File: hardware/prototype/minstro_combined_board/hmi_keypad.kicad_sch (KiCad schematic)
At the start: 34 parts, among them SW401 POWER, SW402 SW_A1, SW403 SW_A2, SW404 SW_A3, SW405 SW_A4, SW406 SW_B1, SW407 SW_B2, SW408 SW_B3, SW409 SW_B4, SW410 SW_C1, SW411 SW_C2, SW412 SW_C3, SW413 SW_C4, SW414 SW_D1, SW415 SW_D2, SW416 SW_D3, SW417 SW_D4

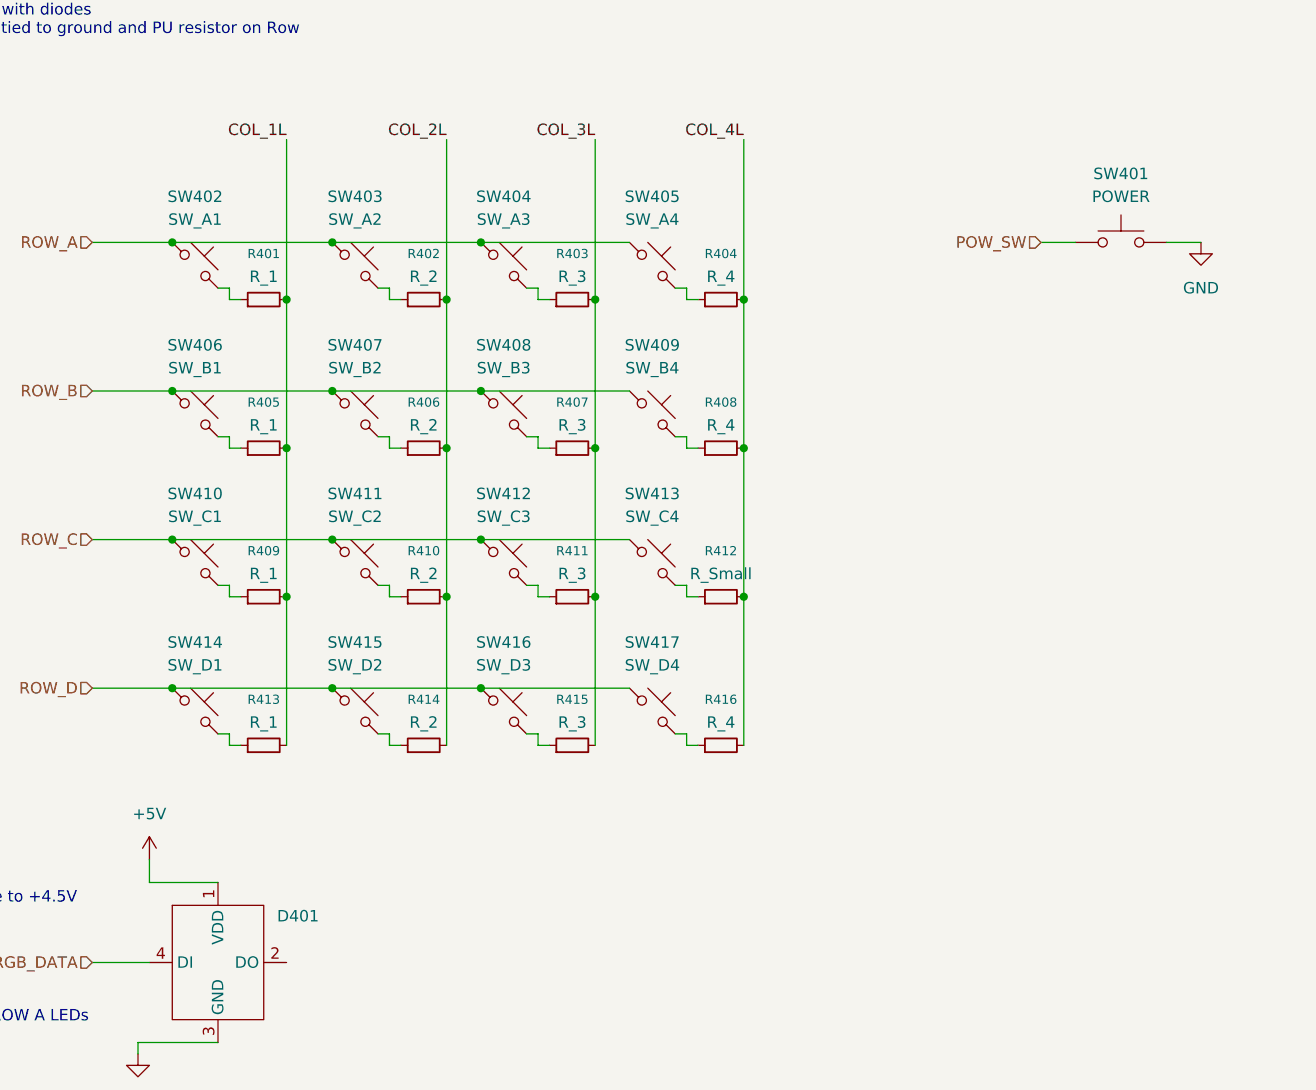
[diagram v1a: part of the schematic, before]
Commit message: Combined board started layout
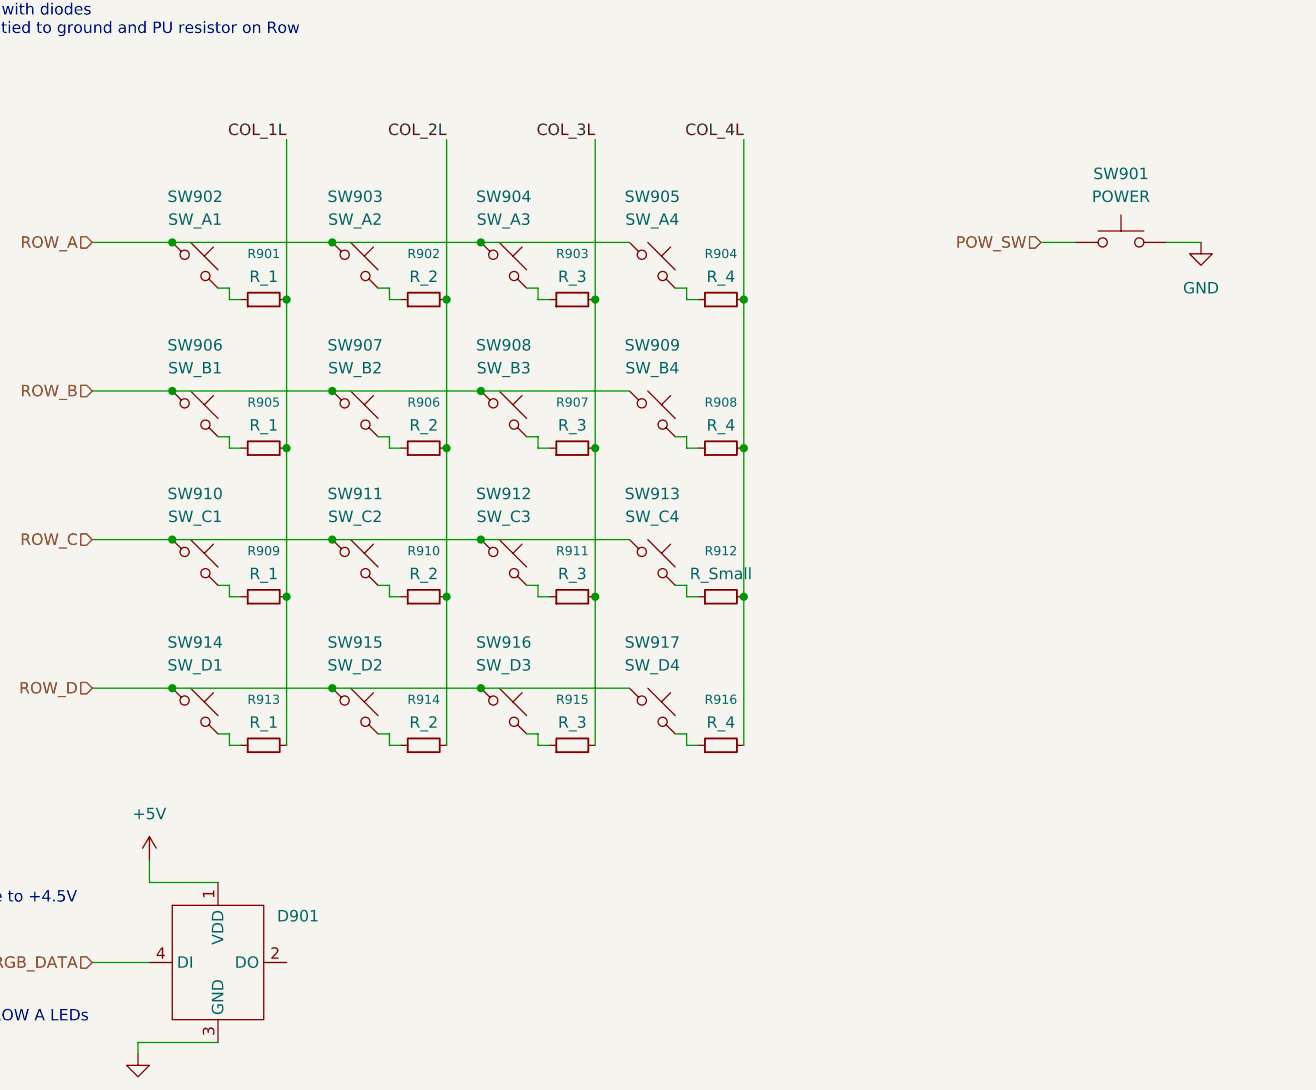
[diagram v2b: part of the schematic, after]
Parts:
- renumbered D401 to D901, R401 to R901, R402 to R902, R403 to R903, R404 to R904, R405 to R905, R406 to R906, R407 to R907, R408 to R908, R409 to R909, R410 to R910, R411 to R911, R412 to R912, R413 to R913, R414 to R914, R415 to R915, R416 to R916, SW401 to SW901, SW402 to SW902, SW403 to SW903, SW404 to SW904, SW405 to SW905, SW406 to SW906, SW407 to SW907, SW408 to SW908, SW409 to SW909, SW410 to SW910, SW411 to SW911, SW412 to SW912, SW413 to SW913, SW414 to SW914, SW415 to SW915, SW416 to SW916, SW417 to SW917

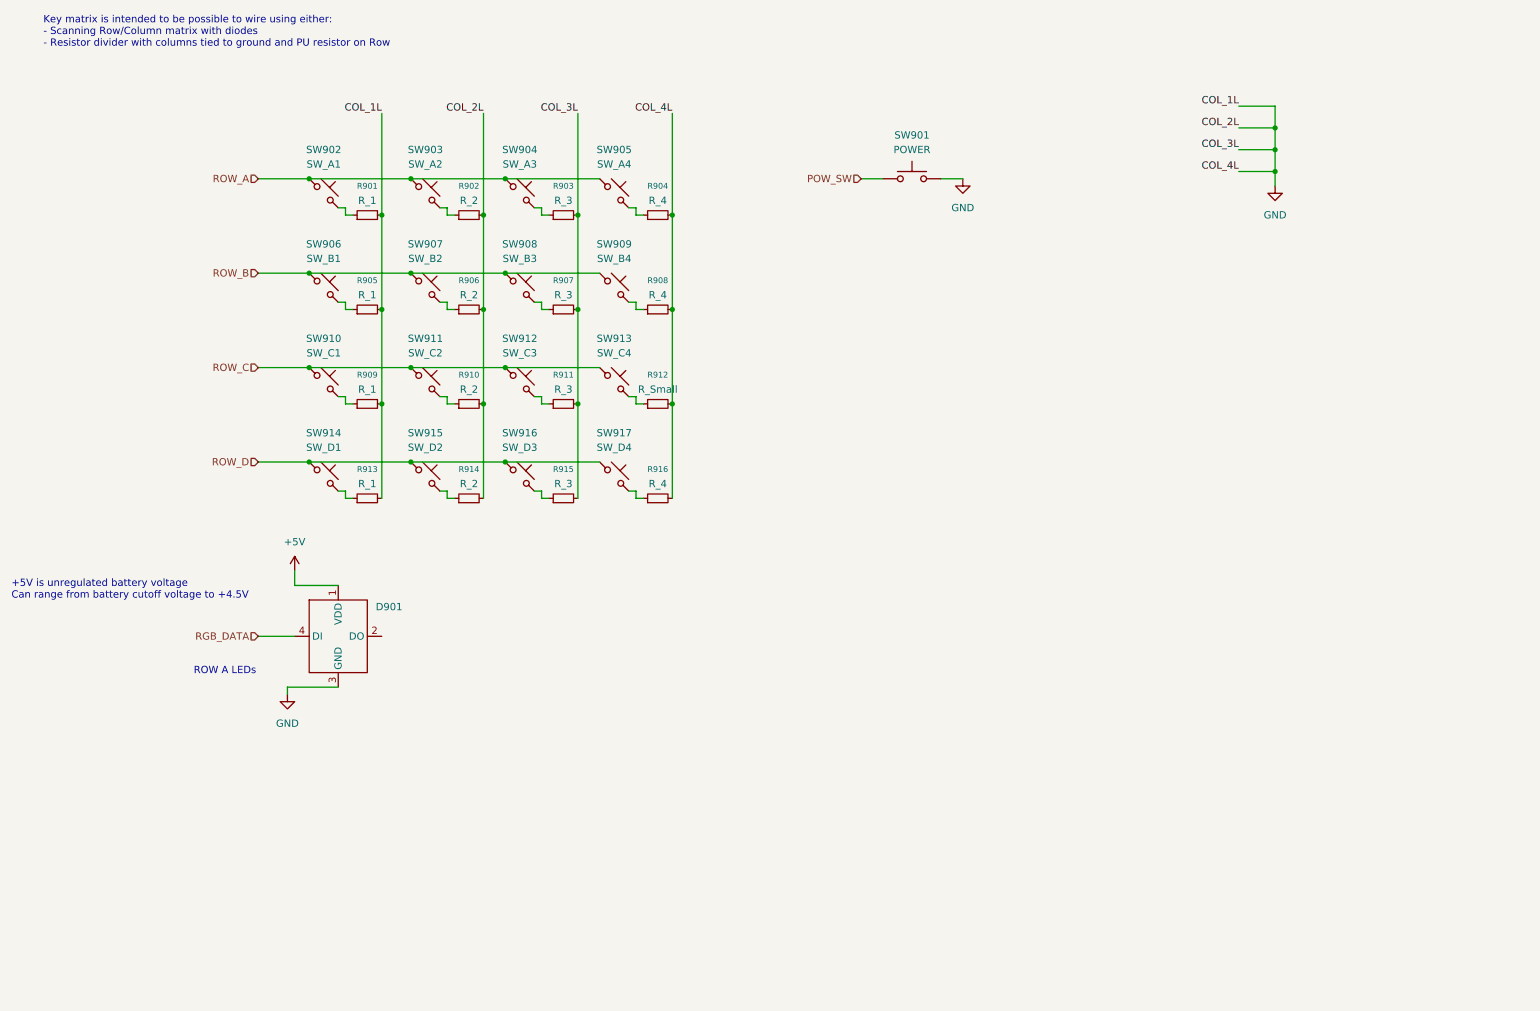
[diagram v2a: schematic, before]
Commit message: Schematic ERC complete
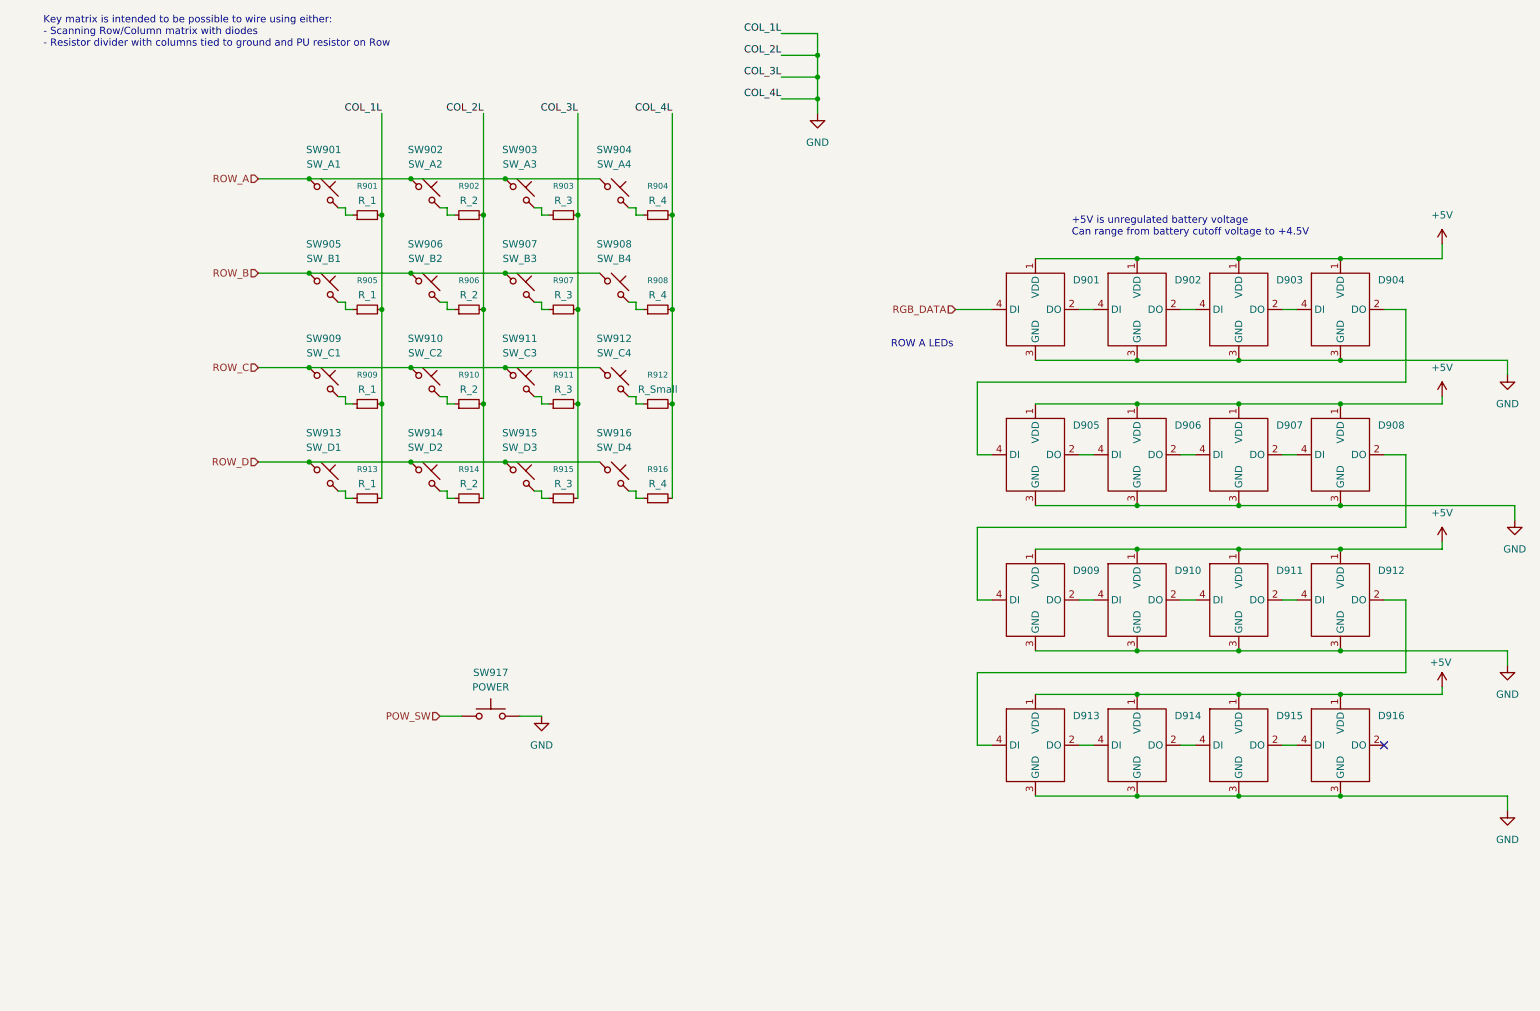
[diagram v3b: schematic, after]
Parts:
- added D902, D903, D904, D905, D906, D907, D908, D909, D910, D911, D912, D913, D914, D915, D916: ~, BVH_LED:SK6812Mini-E_Front, symbol BVH_LED:WS2182-Common
- D901: footprint BVH_LED:XL-0807RGBC-WS2812B -> BVH_LED:SK6812Mini-E_Front
- renumbered SW902 to SW901, SW903 to SW902, SW904 to SW903, SW905 to SW904, SW906 to SW905, SW907 to SW906, SW908 to SW907, SW909 to SW908, SW910 to SW909, SW911 to SW910, SW912 to SW911, SW913 to SW912, SW914 to SW913, SW915 to SW914, SW916 to SW915, SW917 to SW916, SW901 to SW917
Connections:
- net +5V: now also D902.1 (VDD), D903.1 (VDD), D904.1 (VDD), D905.1 (VDD), D906.1 (VDD), D907.1 (VDD), D908.1 (VDD), D909.1 (VDD), D910.1 (VDD), D911.1 (VDD), D912.1 (VDD), D913.1 (VDD), D914.1 (VDD), D915.1 (VDD), D916.1 (VDD)
- net GND: now also D902.3 (GND), D903.3 (GND), D904.3 (GND), D905.3 (GND), D906.3 (GND), D907.3 (GND), D908.3 (GND), D909.3 (GND), D910.3 (GND), D911.3 (GND), D912.3 (GND), D913.3 (GND), D914.3 (GND), D915.3 (GND), D916.3 (GND)
- net at D901.2 (DO): now also D902.4 (DI)
- new net: D914.2 (DO), D915.4 (DI)
- new net: D913.2 (DO), D914.4 (DI)
- new net: D912.2 (DO), D913.4 (DI)
- new net: D904.2 (DO), D905.4 (DI)
- new net: D903.2 (DO), D904.4 (DI)
- new net: D909.2 (DO), D910.4 (DI)
- new net: D908.2 (DO), D909.4 (DI)
- new net: D902.2 (DO), D903.4 (DI)
- new net: D911.2 (DO), D912.4 (DI)
- new net: D910.2 (DO), D911.4 (DI)
- new net: D907.2 (DO), D908.4 (DI)
- new net: D906.2 (DO), D907.4 (DI)
- new net: D915.2 (DO), D916.4 (DI)
- new net: D905.2 (DO), D906.4 (DI)
- no-connect marks 0 -> 1
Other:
- moved on the sheet: D901, SW917

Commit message: Footprint assignment and PCB layout work
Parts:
- R901, R902, R903, R904, R905, R906, R907, R908, R909, R910, R911, R913, R914, R915, R916: footprint (none) -> Resistor_SMD:R_0603_1608Metric
- R912: value R_Small -> R_4; footprint (none) -> Resistor_SMD:R_0603_1608Metric
- SW901, SW902, SW903, SW904, SW905, SW906, SW907, SW908, SW909, SW910, SW911, SW912, SW913, SW914, SW915, SW916: footprint (none) -> BVH_Switches:TacButton_6mm_6mm
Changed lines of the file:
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@@
 			)
 		)
-		(property "Footprint" ""
+		(property "Footprint" "Resistor_SMD:R_0603_1608Metric"
 			(at 93.98 68.58 0)
 			(effects
@@
 			)
 		)
-		(property "Footprint" ""
+		(property "Footprint" "BVH_Switches:TacButton_6mm_6mm"
 			(at 119.38 97.79 0)
 			(effects
@@
 			)
 		)
-		(property "Footprint" ""
+		(property "Footprint" "BVH_Switches:TacButton_6mm_6mm"
 			(at 68.58 81.28 0)
 			(effects
@@
 			)
 		)
-		(property "Footprint" ""
+		(property "Footprint" "BVH_Switches:TacButton_6mm_6mm"
 			(at 119.38 81.28 0)
 			(effects
@@
 			)
 		)
-		(property "Footprint" ""
+		(property "Footprint" "Resistor_SMD:R_0603_1608Metric"
 			(at 110.49 52.07 0)
 			(effects
@@
 			)
 		)
-		(property "Footprint" ""
+		(property "Footprint" "BVH_Switches:TacButton_6mm_6mm"
 			(at 68.58 48.26 0)
 			(effects
@@
 			)
 		)
-		(property "Footprint" ""
+		(property "Footprint" "Resistor_SMD:R_0603_1608Metric"
 			(at 76.2 85.09 0)
 			(effects
@@
 			)
 		)
-		(property "Footprint" ""
+		(property "Footprint" "Resistor_SMD:R_0603_1608Metric"
 			(at 127 52.07 0)
 			(effects
@@
 			)
 		)
-		(property "Footprint" ""
+		(property "Footprint" "Resistor_SMD:R_0603_1608Metric"
 			(at 76.2 68.58 0)
 			(effects
@@
 			)
 		)
-		(property "Footprint" ""
+		(property "Footprint" "BVH_Switches:TacButton_6mm_6mm"
 			(at 102.87 81.28 0)
 			(effects
@@
 			)
 		)
-		(property "Footprint" ""
+		(property "Footprint" "Resistor_SMD:R_0603_1608Metric"
 			(at 110.49 85.09 0)
 			(effects
@@
 			)
 		)
-		(property "Footprint" ""
+		(property "Footprint" "Resistor_SMD:R_0603_1608Metric"
 			(at 93.98 52.07 0)
 			(effects
@@
 			)
 		)
-		(property "Footprint" ""
+		(property "Footprint" "Resistor_SMD:R_0603_1608Metric"
 			(at 76.2 52.07 0)
 			(effects
@@
 			)
 		)
-		(property "Footprint" ""
+		(property "Footprint" "Resistor_SMD:R_0603_1608Metric"
 			(at 76.2 101.6 0)
 			(effects
@@
 			)
 		)
-		(property "Footprint" ""
+		(property "Footprint" "BVH_Switches:TacButton_6mm_6mm"
 			(at 68.58 64.77 0)
 			(effects
@@
 			)
 		)
-		(property "Footprint" ""
+		(property "Footprint" "Resistor_SMD:R_0603_1608Metric"
 			(at 127 68.58 0)
 			(effects
@@
 			)
 		)
-		(property "Footprint" ""
+		(property "Footprint" "BVH_Switches:TacButton_6mm_6mm"
 			(at 102.87 48.26 0)
 			(effects
@@
 			)
 		)
-		(property "Footprint" ""
+		(property "Footprint" "BVH_Switches:TacButton_6mm_6mm"
 			(at 86.36 64.77 0)
 			(effects
@@
 			)
 		)
-		(property "Footprint" ""
+		(property "Footprint" "Resistor_SMD:R_0603_1608Metric"
 			(at 93.98 101.6 0)
 			(effects
@@
 			)
 		)
-		(property "Footprint" ""
+		(property "Footprint" "Resistor_SMD:R_0603_1608Metric"
 			(at 127 101.6 0)
 			(effects
@@
 			)
 		)
-		(property "Value" "R_Small"
+		(property "Value" "R_4"
 			(at 127 82.55 90)
 			(effects
@@
 			)
 		)
-		(property "Footprint" ""
+		(property "Footprint" "Resistor_SMD:R_0603_1608Metric"
 			(at 127 85.09 0)
 			(effects
@@
 			)
 		)
-		(property "Footprint" ""
+		(property "Footprint" "BVH_Switches:TacButton_6mm_6mm"
 			(at 86.36 48.26 0)
 			(effects
@@
 			)
 		)
-		(property "Footprint" ""
+		(property "Footprint" "Resistor_SMD:R_0603_1608Metric"
 			(at 93.98 85.09 0)
 			(effects
@@
 			)
 		)
-		(property "Footprint" ""
+		(property "Footprint" "BVH_Switches:TacButton_6mm_6mm"
 			(at 86.36 81.28 0)
 			(effects
@@
 			)
 		)
-		(property "Footprint" ""
+		(property "Footprint" "BVH_Switches:TacButton_6mm_6mm"
 			(at 86.36 97.79 0)
 			(effects
@@
 			)
 		)
-		(property "Footprint" ""
+		(property "Footprint" "BVH_Switches:TacButton_6mm_6mm"
 			(at 102.87 97.79 0)
 			(effects
@@
 			)
 		)
-		(property "Footprint" ""
+		(property "Footprint" "BVH_Switches:TacButton_6mm_6mm"
 			(at 119.38 64.77 0)
 			(effects
@@
 			)
 		)
-		(property "Footprint" ""
+		(property "Footprint" "BVH_Switches:TacButton_6mm_6mm"
 			(at 119.38 48.26 0)
 			(effects
@@
 			)
 		)
-		(property "Footprint" ""
+		(property "Footprint" "BVH_Switches:TacButton_6mm_6mm"
 			(at 68.58 97.79 0)
 			(effects
@@
 			)
 		)
-		(property "Footprint" ""
+		(property "Footprint" "Resistor_SMD:R_0603_1608Metric"
 			(at 110.49 68.58 0)
 			(effects
@@
 			)
 		)
-		(property "Footprint" ""
+		(property "Footprint" "BVH_Switches:TacButton_6mm_6mm"
 			(at 102.87 64.77 0)
 			(effects
@@
 			)
 		)
-		(property "Footprint" ""
+		(property "Footprint" "Resistor_SMD:R_0603_1608Metric"
 			(at 110.49 101.6 0)
 			(effects
